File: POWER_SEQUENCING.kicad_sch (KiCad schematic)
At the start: 27 parts, among them SW2 SW_Omron_B3FS, U20 74LVC1G08, U21 74LVC1G08, U22 LM397, U23 74LVC1G17, U29 74LVC1G32, U30 74LVC1G08

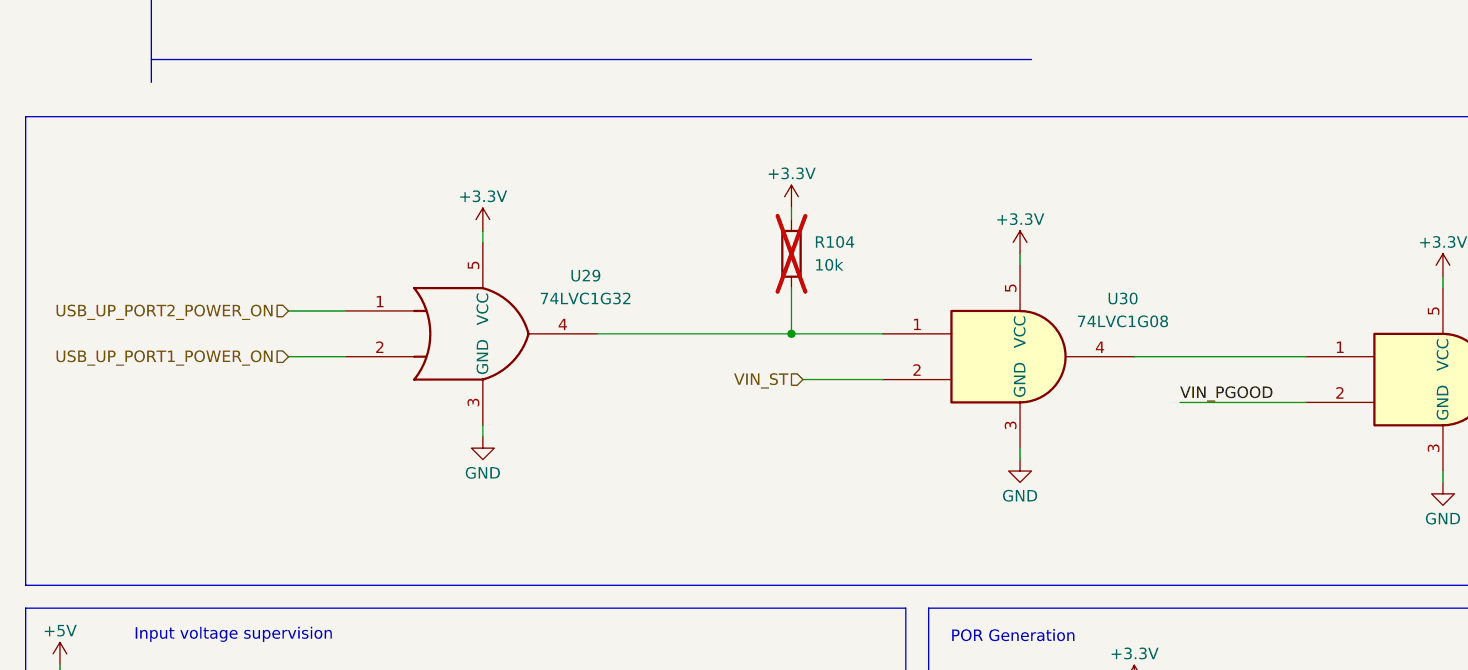
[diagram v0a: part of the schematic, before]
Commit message: Power In Circuitry extended for more current
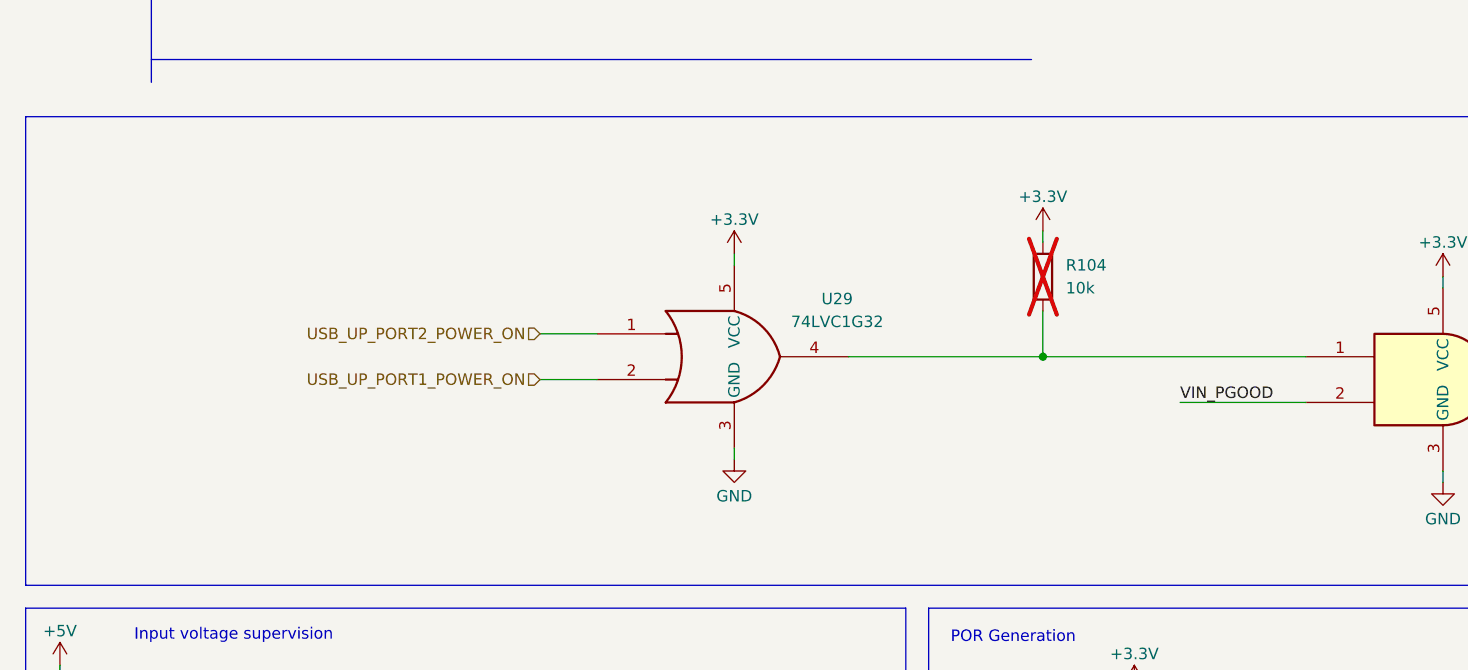
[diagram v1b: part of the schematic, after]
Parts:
- removed U30: 74LVC1G08, Package_TO_SOT_SMD:SOT-23-5, symbol 74xGxx:74LVC1G08
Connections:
- net at U21.1: now also R104.2, U29.4
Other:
- moved on the sheet: R104, U29
